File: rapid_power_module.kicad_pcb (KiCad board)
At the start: 4 copper layers, 80 x 136 mm, 209 parts, among them J1 Conn_02x04_Top_Bottom, J10 JST-GH 4Pin, J11 SWD Header, J12 SWD Header, J16 USB_C_Receptacle_USB2.0, J17 TC2050, J2 Conn_02x03_Odd_Even, J3 Conn_02x04_Top_Bottom, J4 Conn_02x03_Odd_Even, J6 Molex MicroFit 2x2, J7 Molex MicroFit 2x2, J8 Molex MicroFit 2x2, J9 Conn_02x04_Top_Bottom, Q1 AOSP21321, Q12 AOSP21321, Q4 HiDRV1, Q5 LoDRV1, Q6 HiDRV2, Q7 LoDRV2, SW1 KMR721NGLFS, SW2 KMR721NGLFS, U1 BQ25756RRVR, U10 L7805, U11 MCP2562-E-SN, U12 STM32F105RCTx, U13 AZ1117I-3.3, U14 TPD4E1U06, U15 TPD4E1U06, U2 CYPD3177-24LQ, U3 BQ76952PFBR, Y3 8MHz 12pF

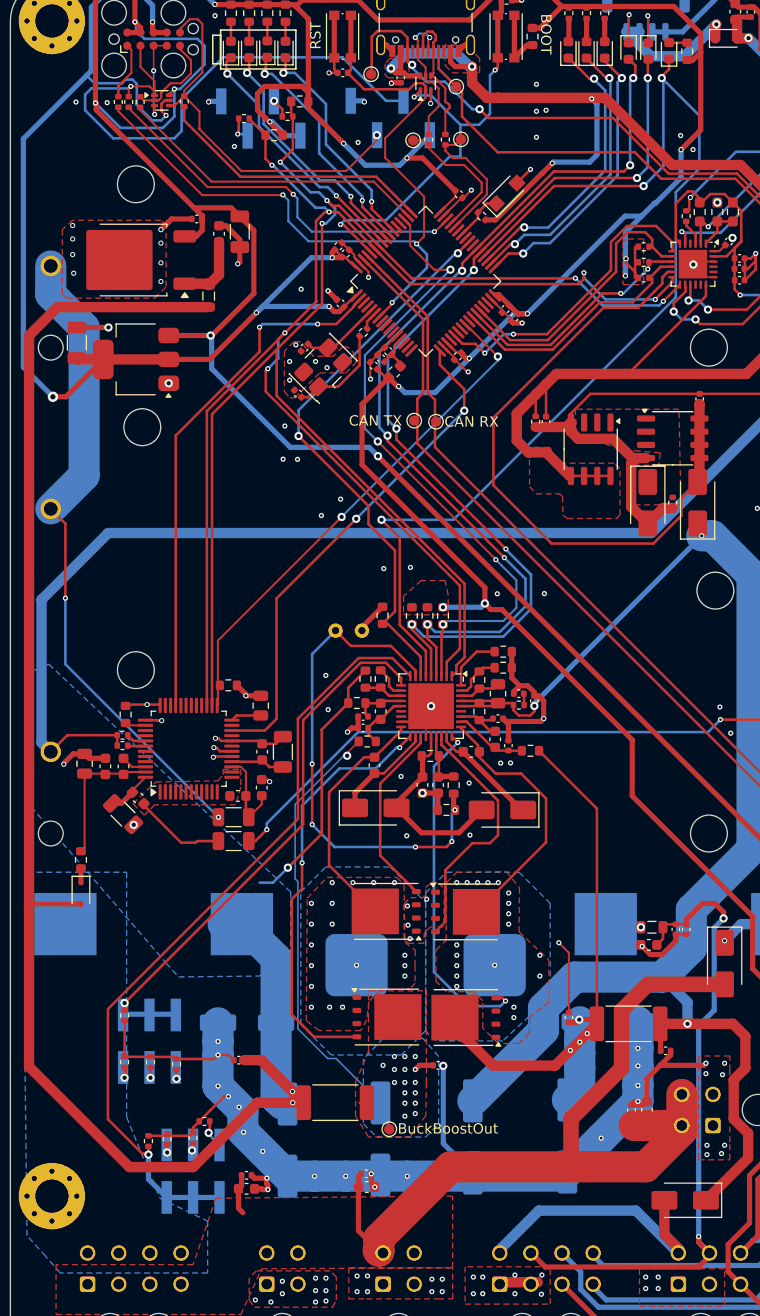
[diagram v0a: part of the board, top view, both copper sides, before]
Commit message: finish routing and silkscreen improvements
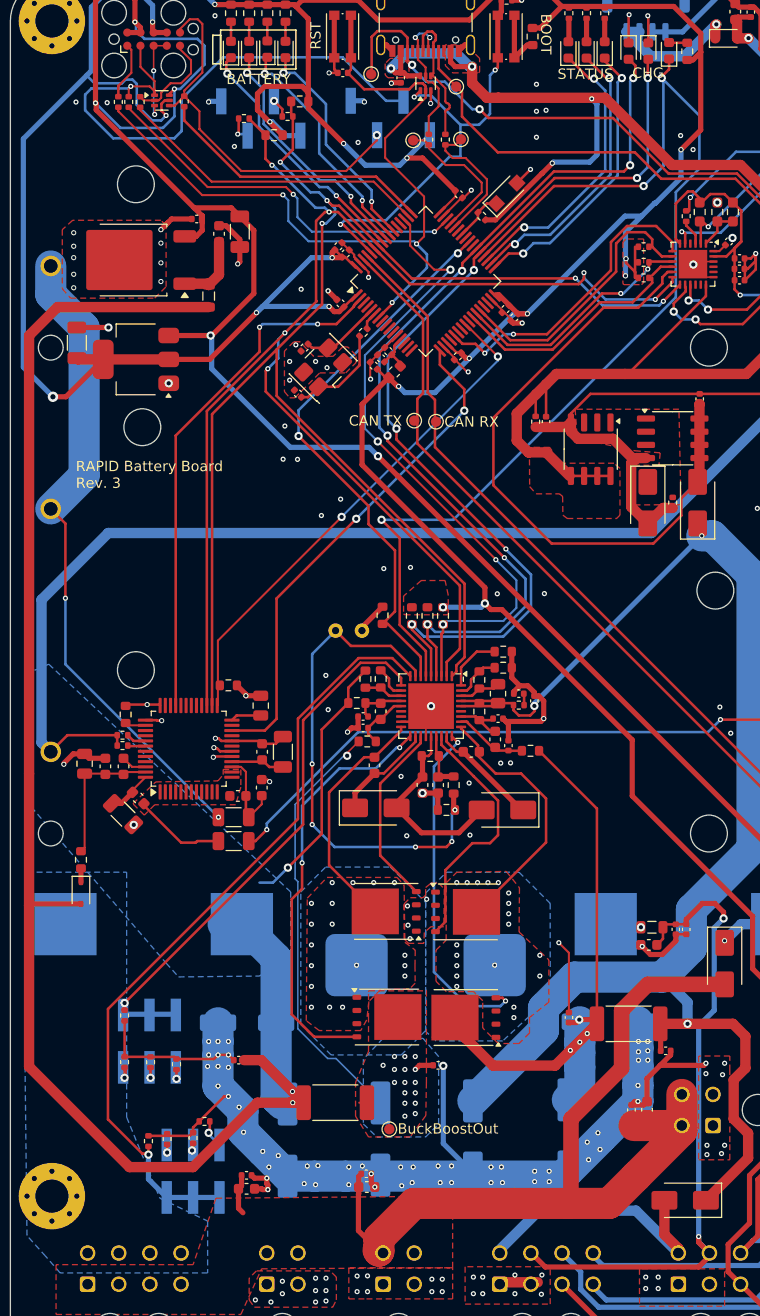
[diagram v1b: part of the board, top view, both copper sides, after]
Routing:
- net +VSW: track 83.2 -> 86.9 mm
- net GND: track 313.2 -> 312.9 mm, vias 155 -> 192
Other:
- board text added: "BATTERY"
- board text added: "CHG"
- board text added: "JLCJLCJLCJLC"
- board text added: "RAPID Battery Board Rev. 3"
- board text added: "STATUS"

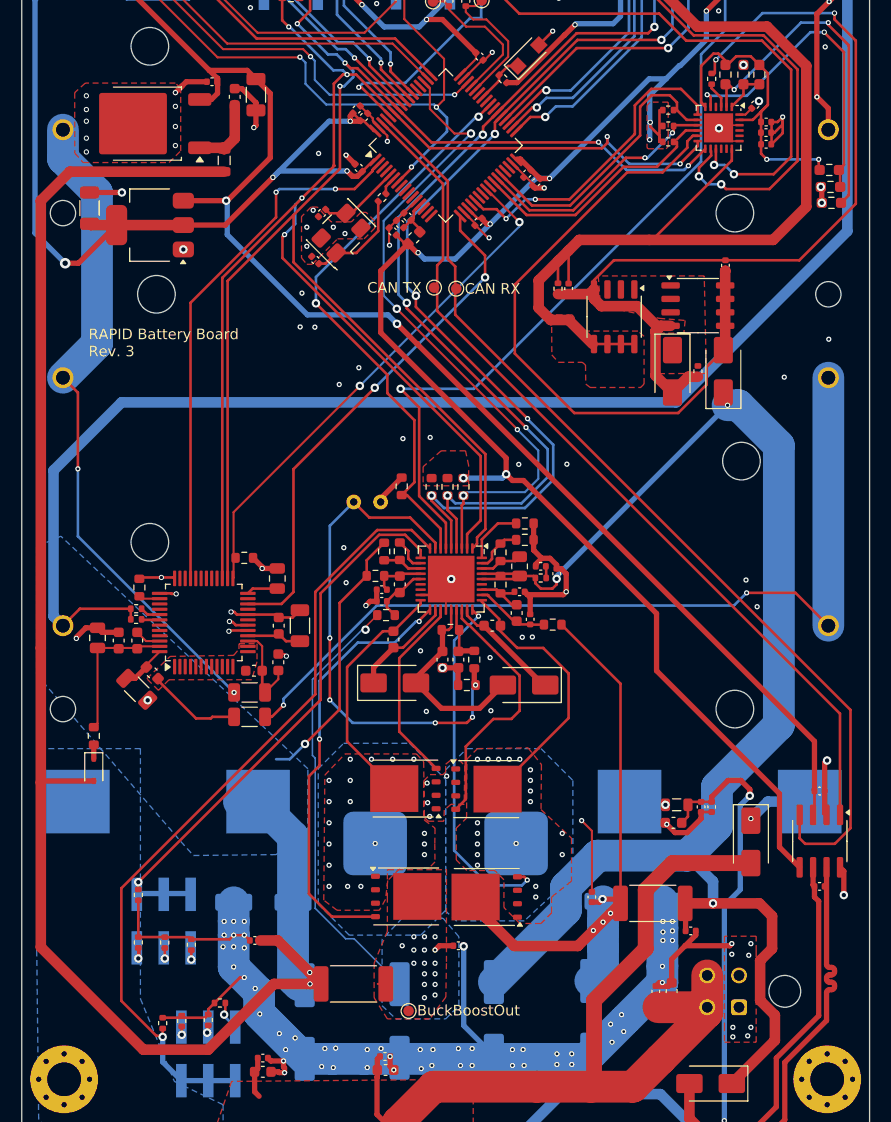
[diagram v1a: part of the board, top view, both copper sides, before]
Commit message: Finishing touches (Zone optimizations to reduce antenna effect, wider battery connection zones)
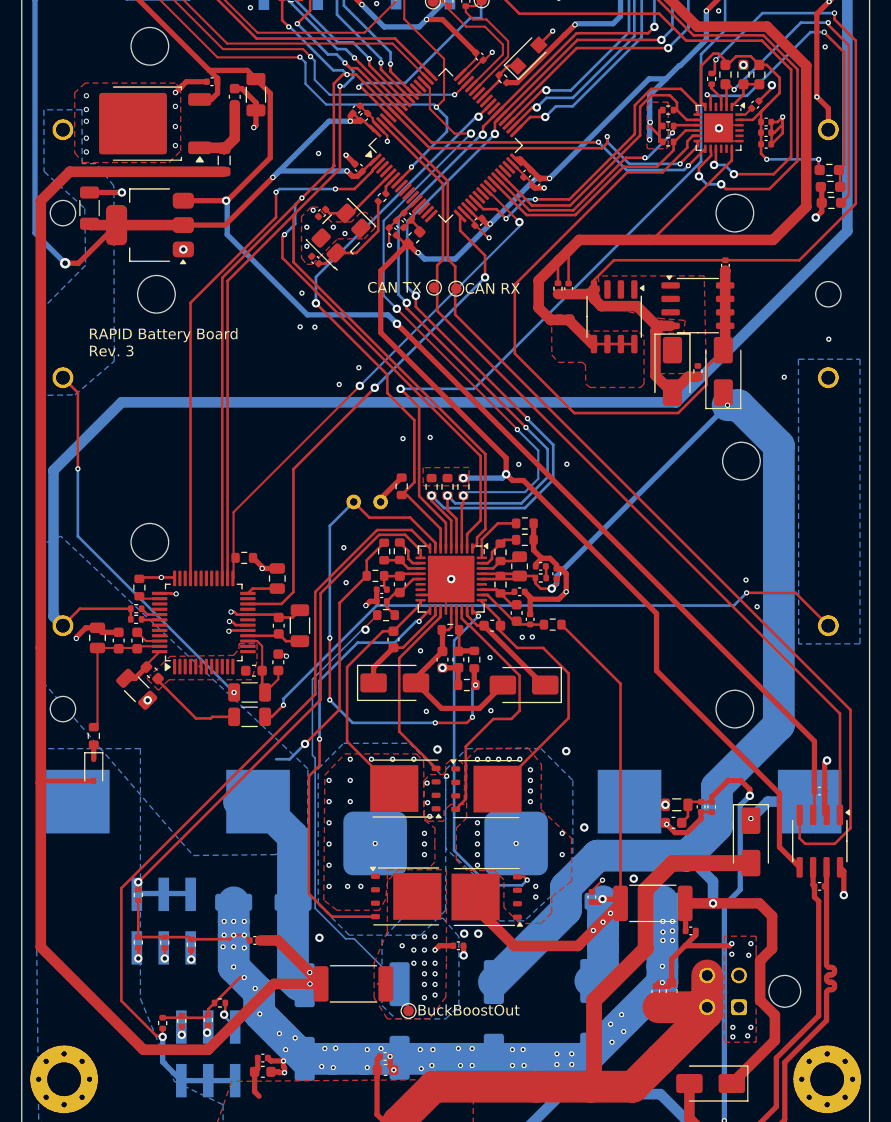
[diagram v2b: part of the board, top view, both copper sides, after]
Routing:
- net Net-(BT2--): track 62.4 -> 36.4 mm
- net Net-(BT1--): track 83.0 -> 59.6 mm
- net GND: track 312.9 -> 300.7 mm, vias 192 -> 198
- net PD_VDDD: track 30.1 -> 31.4 mm
- net V_in: track 143.1 -> 144.2 mm
- added copper zone on B.Cu, net Net-(BT1--)
- added copper zone on B.Cu, net Net-(BT2--)

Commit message: Replace wrong battery manager footprint
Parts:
- R66, R67: footprint Resistor_SMD:R_0603_1608Metric -> Resistor_SMD:R_0402_1005Metric
- U1: footprint Package_DFN_QFN:Texas_RHH0036C_VQFN-36-1EP_6x6mm_P0.5mm_EP4.4x4.4mm -> Package_DFN_QFN:QFN-36-1EP_5x6mm_P0.5mm_EP3.6x4.6mm
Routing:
- net V_in: track 144.2 -> 141.6 mm
- net GND: track 300.7 -> 303.1 mm
- net REGN: track 5.06 -> 5.97 mm
- net ACN: track 7.08 -> 6.27 mm
- net HIDRV1: track 33.4 -> 34.1 mm
- net Net-(J4-Pin_2): track 76.2 -> 76.9 mm
- net LODRV1: track 24.6 -> 25.2 mm
- net PG: track 109.2 -> 109.7 mm
- net Net-(U1-TS): track 48.5 -> 49.1 mm
- net BTST1: track 10.5 -> 11.0 mm
- net CE: track 55.0 -> 55.5 mm
- net STAT2: track 92.5 -> 93.1 mm
- net STAT1: track 89.3 -> 89.8 mm

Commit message: Add basic running embassy loop
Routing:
- added copper zone on F.Cu, net Net-(J9-Pin_5)
- removed copper zone on B.Cu, net Net-(J9-Pin_5)
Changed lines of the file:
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@@
 			(psa4output no)
 			(plot_black_and_white yes)
-			(plotinvisibletext no)
 			(sketchpadsonfab no)
 			(plotpadnumbers no)
@@
 			(keep_text_aligned yes)
 		)
-		(gr_text "40,0000 mm"
+		(gr_text "40.0000 mm"
 			(at 115 13.7 0)
 			(layer "F.Cu")
@@
 			(keep_text_aligned yes)
 		)
-		(gr_text "68,0000 mm"
+		(gr_text "68.0000 mm"
 			(at 87.2 56 90)
 			(layer "F.Cu")
@@
 			(keep_text_aligned yes)
 		)
-		(gr_text "80,0000 mm"
+		(gr_text "80.0000 mm"
 			(at 132.7 166.8 0)
 			(layer "F.Cu")
@@
 			(keep_text_aligned yes)
 		)
-		(gr_text "136,0000 mm"
+		(gr_text "136.0000 mm"
 			(at 63.8 84.199988 90)
 			(layer "F.Cu")
@@
 	)
 	(zone
+		(net 161)
+		(net_name "Net-(J9-Pin_5)")
+		(layer "F.Cu")
+		(hatch edge 0.5)
+		(priority 22)
+		(connect_pads
+			(clearance 0.3)
+		)
+		(min_thickness 0.25)
+		(filled_areas_thickness no)
+		(fill
+			(thermal_gap 0.5)
+			(thermal_bridge_width 0.5)
+		)
+		(polygon
+			(pts
+				(xy 114 146.6) (xy 128.2 146.6) (xy 129.6 145) (xy 131.4 143) (xy 131.581274 127.215076) (xy 131.4 108)
+				(xy 121.8 108) (xy 121.8 131.6) (xy 118.6 139.4) (xy 114 141.6)
+			)
+		)
+	)
+	(zone
 		(net 71)
 		(net_name "GND")
@@
 			)
 		)
-	)
-	(zone
-		(net 161)
-		(net_name "Net-(J9-Pin_5)")
-		(layer "B.Cu")
-		(hatch edge 0.5)
-		(priority 22)
-		(connect_pads
-			(clearance 0.3)
-		)
-		(min_thickness 0.25)
-		(filled_areas_thickness no)
-		(fill yes
-			(thermal_gap 0.5)
-			(thermal_bridge_width 0.5)
-		)
-		(polygon
-			(pts
-				(xy 114 146.6) (xy 99.8 146.6) (xy 98.4 145) (xy 96.6 143) (xy 96.418726 127.215076) (xy 96.6 108)
-				(xy 106.2 108) (xy 106.2 131.6) (xy 109.4 139.4) (xy 114 141.6)
-			)
-		)

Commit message: fix broken trace
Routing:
- added copper zone on B.Cu, net Net-(J9-Pin_5)
- removed copper zone on F.Cu, net Net-(J9-Pin_5)
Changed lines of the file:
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@@
 			(keep_text_aligned yes)
 		)
-		(gr_text "40.0000 mm"
+		(gr_text "40,0000 mm"
 			(at 115 13.7 0)
 			(layer "F.Cu")
@@
 			(keep_text_aligned yes)
 		)
-		(gr_text "68.0000 mm"
+		(gr_text "68,0000 mm"
 			(at 87.2 56 90)
 			(layer "F.Cu")
@@
 			(keep_text_aligned yes)
 		)
-		(gr_text "80.0000 mm"
+		(gr_text "80,0000 mm"
 			(at 132.7 166.8 0)
 			(layer "F.Cu")
@@
 			(keep_text_aligned yes)
 		)
-		(gr_text "136.0000 mm"
+		(gr_text "136,0000 mm"
 			(at 63.8 84.199988 90)
 			(layer "F.Cu")
@@
 	)
 	(zone
-		(net 161)
-		(net_name "Net-(J9-Pin_5)")
-		(layer "F.Cu")
-		(hatch edge 0.5)
-		(priority 22)
-		(connect_pads
-			(clearance 0.3)
-		)
-		(min_thickness 0.25)
-		(filled_areas_thickness no)
-		(fill
-			(thermal_gap 0.5)
-			(thermal_bridge_width 0.5)
-		)
-		(polygon
-			(pts
-				(xy 114 146.6) (xy 128.2 146.6) (xy 129.6 145) (xy 131.4 143) (xy 131.581274 127.215076) (xy 131.4 108)
-				(xy 121.8 108) (xy 121.8 131.6) (xy 118.6 139.4) (xy 114 141.6)
-			)
-		)
-	)
-	(zone
 		(net 71)
 		(net_name "GND")
@@
 			)
 		)
+	)
+	(zone
+		(net 161)
+		(net_name "Net-(J9-Pin_5)")
+		(layer "B.Cu")
+		(hatch edge 0.5)
+		(priority 22)
+		(connect_pads
+			(clearance 0.3)
+		)
+		(min_thickness 0.25)
+		(filled_areas_thickness no)
+		(fill yes
+			(thermal_gap 0.5)
+			(thermal_bridge_width 0.5)
+		)
+		(polygon
+			(pts
+				(xy 112.815384 146.537793) (xy 98.615384 146.537793) (xy 97.215384 144.937793) (xy 95.415384 142.937793)
+				(xy 95.23411 127.152869) (xy 95.415384 107.937793) (xy 105.015384 107.937793) (xy 105.015384 131.537793)
+				(xy 108.215384 139.337793) (xy 112.815384 141.537793)
+			)
+		)

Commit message: added missing footprints and validated all lcsc numbers; started pcb-layouting
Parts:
- removed BT3: Battery_Cell, Inductor Wuerth:BAT_1043
- removed C13, C37, C38, C44, C45: 100n, Capacitor_SMD:C_0402_1005Metric
- removed C20, C65: 1u, Capacitor_SMD:C_0402_1005Metric
- removed C39, C43, C47, C48: 470n, Capacitor_SMD:C_0603_1608Metric
- removed C49: 47n, Capacitor_SMD:C_0603_1608Metric
- removed C86, C90: 10u, Capacitor_SMD:C_0603_1608Metric
- removed C87, C91: 10n, Capacitor_SMD:C_0402_1005Metric
- removed D16, D21, D23, D7: green, LED_SMD:LED_0603_1608Metric
- removed D20: yellow, LED_SMD:LED_0603_1608Metric
- removed D22: red, LED_SMD:LED_0603_1608Metric
- removed D24: Vz = 3.6V, Diode_SMD:Nexperia_CFP3_SOD-123W
- removed D9: ~, Diode_SMD:D_SOD-323
- removed FB3: 120R, Inductor_SMD:L_0805_2012Metric
- removed J10: JST-GH 4Pin, Connector_JST:JST_GH_SM04B-GHS-TB_1x04-1MP_P1.25mm_Horizontal
- removed J11: SWD Header, Connector_PinHeader_2.54mm:PinHeader_1x04_P2.54mm_Vertical_SMD_Pin1Left
- removed J16: USB_C_Receptacle_USB2.0, Connector_USB:USB_C_Receptacle_Palconn_UTC16-G
- removed J8: Molex MicroFit 2x2, Connector_Molex:Molex_Micro-Fit_3.0_43045-0400_2x02_P3.00mm_Horizontal
- removed J9: Conn_02x04_Top_Bottom, Connector_Molex:Molex_Micro-Fit_3.0_43045-0800_2x04_P3.00mm_Horizontal
- removed Q12: AOSP21321, Package_SO:SO-8_3.9x4.9mm_P1.27mm
- removed Q4: HiDRV1, Package_TO_SOT_SMD:TDSON-8-1
- removed Q5: LoDRV1, Package_TO_SOT_SMD:TDSON-8-1
- removed Q6: HiDRV2, Package_TO_SOT_SMD:TDSON-8-1
- removed Q7: LoDRV2, Package_TO_SOT_SMD:TDSON-8-1
- removed R19, R48: 0R, Resistor_SMD:R_0603_1608Metric_Pad0.98x0.95mm_HandSolder
- removed R20: 20, Resistor_SMD:R_1206_3216Metric
- removed R21: 100, Resistor_SMD:R_0603_1608Metric
- removed R22: 10R, Resistor_SMD:R_0603_1608Metric
- removed R23: 4k7, Resistor_SMD:R_0603_1608Metric
- removed R24: 100k, Resistor_SMD:R_0603_1608Metric
- removed R25, R94, R97: 20k, Resistor_SMD:R_0402_1005Metric
- removed R27: 50k, Resistor_SMD:R_0402_1005Metric
- removed R28: 250k, Resistor_SMD:R_0603_1608Metric
- removed R31: 50k, Resistor_SMD:R_0603_1608Metric
- removed R33: 300k, Resistor_SMD:R_0603_1608Metric
- removed R37, R41, R79, R80: 10, Resistor_SMD:R_0603_1608Metric
- removed R38, R65: 5m, Resistor_SMD:R_2512_6332Metric_Pad1.40x3.35mm_HandSolder
- removed R39, R45: 4k7, Resistor_SMD:R_0402_1005Metric
- removed R40, R42, R46, R95: 10k, Resistor_SMD:R_0402_1005Metric
- removed R43: 68k, Resistor_SMD:R_0603_1608Metric
- removed R44: 1000k, Resistor_SMD:R_0805_2012Metric
- removed R47: dnp, Resistor_SMD:R_0603_1608Metric_Pad0.98x0.95mm_HandSolder
- removed R64, R69, R70, R72, R91: 10k, Resistor_SMD:R_0603_1608Metric
- removed R73, R75: 22R, Resistor_SMD:R_0402_1005Metric
- removed R83: 49k9, Resistor_SMD:R_0402_1005Metric
- removed R89, R90: 1k, Resistor_SMD:R_0402_1005Metric
- removed R96: 5k1, Resistor_SMD:R_0402_1005Metric
- removed R98: 15k, Resistor_SMD:R_0402_1005Metric
- removed TP1: BuckBoostOut, TestPoint:TestPoint_Pad_D1.0mm
- removed TP2: TP_CAN_TX, TestPoint:TestPoint_Pad_D1.0mm
- removed TP3: TP_CAN_RX, TestPoint:TestPoint_Pad_D1.0mm
- removed TP4: TP_USB_D+, TestPoint:TestPoint_Pad_D1.0mm
- removed TP5: TP_USB_D-, TestPoint:TestPoint_Pad_D1.0mm
- removed TP6: TP_USB_CC2, TestPoint:TestPoint_Pad_D1.0mm
- removed TP7: TP_USB_CC1, TestPoint:TestPoint_Pad_D1.0mm
- removed U14: TPD4E1U06, Package_TO_SOT_SMD:SOT-563
- removed U3: BQ76952PFBR, Package_QFP:TQFP-48_7x7mm_P0.5mm
- added BT4: Battery_Cell, Inductor Wuerth:BAT_1043, B.Cu at (123.7, 108.8)
- added C27: 10u, Capacitor_SMD:C_0603_1608Metric, F.Cu at (391.6, 12.6)
- added C28: 10u, Capacitor_SMD:C_0603_1608Metric, F.Cu at (-1.82, 233.2)
- added C29: 10n, Capacitor_SMD:C_0402_1005Metric, F.Cu at (-2.09, 229.8)
- added C30: 100n, Capacitor_SMD:C_0402_1005Metric, F.Cu at (387.6, 18.1)
- added C31: 10u, Capacitor_SMD:C_0603_1608Metric, F.Cu at (391.6, 11.0)
- added C32: 10u, Capacitor_SMD:C_0603_1608Metric, F.Cu at (391.6, 9.45)
- added C33: 10u, Capacitor_SMD:C_0603_1608Metric, F.Cu at (391.6, 7.90)
- added C34: 10u, Capacitor_SMD:C_0603_1608Metric, F.Cu at (391.6, 6.35)
- added D10: ~, Diode_SMD:D_SMA, F.Cu at (122.3, -77.2)
- added D3: green, LED_SMD:LED_0805_2012Metric, F.Cu at (160.5, -70.0)
- added F2: 20A, Fuse:Fuseholder_Cylinder-5x20mm_Wuerth_696103101002-SMD_Horizontal_Open, F.Cu at (135.7, 114.8)
- added J5: Molex MicroFit 2x2, Connector_Molex:Molex_Micro-Fit_3.0_43045-0400_2x02_P3.00mm_Horizontal, B.Cu at (156.0, 125.0)
- added Q2: NMOS, Package_TO_SOT_THT:TO-220-3_Horizontal_TabDown, F.Cu at (387.9, 23.4)
- added R10: 1k, Resistor_SMD:R_0402_1005Metric, F.Cu at (155.7, -65.8)
- added R13: 1k, Resistor_SMD:R_0402_1005Metric, F.Cu at (162.8, -68.0)
- added R_IN1: 75, Resistor_SMD:R_0603_1608Metric, F.Cu at (-52.1, 71.9)
- added R_IN2: 75, Resistor_SMD:R_0603_1608Metric, F.Cu at (-51.4, 74.1)
- added R_IN3: 75, Resistor_SMD:R_0603_1608Metric, F.Cu at (-51.4, 77.2)
- added R_IN4: 75, Resistor_SMD:R_0603_1608Metric, F.Cu at (-51.4, 80.2)
- added R_LD1: 453k, Resistor_SMD:R_0402_1005Metric, F.Cu at (-42.2, 76.0)
- added R_SNS1: 1m, Resistor_SMD:R_2512_6332Metric, F.Cu at (-46.7, 79.8)
- added R_TS_PU1: 10k, Resistor_SMD:R_0402_1005Metric, F.Cu at (-42.2, 73.3)
- C10, C11: value 1u -> 100n
- C14: value 220n -> 2.2u; footprint Capacitor_SMD:C_0603_1608Metric -> Capacitor_SMD:C_0805_2012Metric
- C15: value 220n -> 100n; footprint Capacitor_SMD:C_0603_1608Metric -> Capacitor_SMD:C_0402_1005Metric
- C16: value 220n -> 1n; footprint Capacitor_SMD:C_0603_1608Metric -> Capacitor_SMD:C_0402_1005Metric
- C17: value 220n -> 1u; footprint Capacitor_SMD:C_0603_1608Metric -> Capacitor_SMD:C_0402_1005Metric
- C18: value 470n -> 1u; footprint Capacitor_SMD:C_0603_1608Metric -> Capacitor_SMD:C_0402_1005Metric
- C19: value 1u -> 100n; footprint Capacitor_SMD:C_0805_2012Metric -> Capacitor_SMD:C_0402_1005Metric
- C2, C4, C5: value 82u -> 10u; footprint Capacitor_SMD:CP_Elec_8x6.9 -> Capacitor_SMD:C_0603_1608Metric; moved to F.Cu
- C21: value 2u2 -> 100n; footprint Capacitor_SMD:C_0805_2012Metric -> Capacitor_SMD:C_0402_1005Metric
- C22: value 0.47uF -> 100n
- C23: value 3u3 -> 10u; footprint Capacitor_SMD:C_0402_1005Metric -> Capacitor_SMD:C_0603_1608Metric
- C24: value 100p -> 100n; footprint Capacitor_SMD:C_0603_1608Metric -> Capacitor_SMD:C_0402_1005Metric
- C26: value 100n -> 4u7
- C3: value 100n -> 10u; footprint Capacitor_SMD:C_0402_1005Metric -> Capacitor_SMD:C_0603_1608Metric
- C58: value 470n -> 330n
- C6: value 82u -> 100n; footprint Capacitor_SMD:CP_Elec_8x6.9 -> Capacitor_SMD:C_0402_1005Metric; moved to F.Cu
- C7, C8: footprint Capacitor_SMD:CP_Elec_6.3x5.9 -> Capacitor_SMD:C_0603_1608Metric; moved to F.Cu
- C9: value 1u -> 47n; footprint Capacitor_SMD:C_0402_1005Metric -> Capacitor_SMD:C_0603_1608Metric
- D1: value D -> 12V; footprint Diode_SMD:D_SMA -> Diode_SMD:D_SOD-523
- D18, D19, D5: footprint LED_SMD:LED_0603_1608Metric -> LED_SMD:LED_0805_2012Metric
- D2: value D -> red; footprint Diode_SMD:D_SMA -> LED_SMD:LED_0603_1608Metric
- D4: value ~ -> green; footprint Diode_SMD:D_SOD-323 -> LED_SMD:LED_0805_2012Metric
- D6: value ~ -> green; footprint Diode_SMD:D_SMA -> LED_SMD:LED_0805_2012Metric
- F1: moved to F.Cu
- F3: value 20A -> 5A; moved to F.Cu
- J17: moved to B.Cu
- J2, J4: value Conn_02x03_Odd_Even -> Molex MicroFit 2x2; footprint Connector_PinHeader_2.54mm:PinHeader_2x03_P2.54mm_Vertical_SMD -> Connector_Molex:Molex_Micro-Fit_3.0_43045-0400_2x02_P3.00mm_Horizontal; moved to F.Cu
- L2: value 5u6 -> 1u; footprint Inductor Wuerth:Wuerth 7443557560 -> Inductor_SMD_Wurth:L_Wurth_WE-LQSH-3012; moved to F.Cu
- Q1: value AOSP21321 -> NMOS; footprint Package_SO:SO-8_3.9x4.9mm_P1.27mm -> Package_TO_SOT_THT:TO-220-3_Horizontal_TabDown
- R1: value 2.4 -> 2; footprint Resistor_SMD:R_0402_1005Metric -> Resistor_SMD:R_0603_1608Metric
- R11, R12: value 20 -> 1k; footprint Resistor_SMD:R_1206_3216Metric -> Resistor_SMD:R_0402_1005Metric
- R14, R15, R16, R34: footprint Resistor_SMD:R_0603_1608Metric -> Resistor_SMD:R_0402_1005Metric
- R17: value 1k -> 100
- R18: value dnp -> 100; footprint Resistor_SMD:R_0603_1608Metric_Pad0.98x0.95mm_HandSolder -> Resistor_SMD:R_0603_1608Metric
- R2: value 20 -> 10k5; footprint Resistor_SMD:R_1206_3216Metric -> Resistor_SMD:R_0603_1608Metric
- R3: value 35k -> 10k5
- R32: value 4k -> 5k24
- R4: value 10k -> 294; footprint Resistor_SMD:R_0402_1005Metric -> Resistor_SMD:R_0603_1608Metric
- R5: value 1k -> 100; footprint Resistor_SMD:R_0402_1005Metric -> Resistor_SMD:R_0603_1608Metric
- R6: value 0R -> 20k; footprint Resistor_SMD:R_0603_1608Metric_Pad0.98x0.95mm_HandSolder -> Resistor_SMD:R_0603_1608Metric
- R66, R67: value 4.7k -> 10k
- R7: value dnp -> 2k2; footprint Resistor_SMD:R_0603_1608Metric_Pad0.98x0.95mm_HandSolder -> Resistor_SMD:R_0603_1608Metric
- R8: value 49k9 -> 1k
- R82: value 22k -> 30k31; footprint Resistor_SMD:R_0603_1608Metric -> Resistor_SMD:R_0805_2012Metric
- SW1, SW2: value KMR721NGLFS -> TS342A2P; footprint Button_Switch_SMD:SW_Push_1P1T_NO_CK_KMR2 -> Button_Switch_SMD:SW_Push_SPST_NO_Alps_SKRK
- TH1: footprint Resistor_THT:R_Axial_DIN0204_L3.6mm_D1.6mm_P2.54mm_Vertical -> Resistor_SMD:R_0603_1608Metric; moved to F.Cu
- U1: value BQ25756RRVR -> BQ7791500PWR; footprint Package_DFN_QFN:QFN-36-1EP_5x6mm_P0.5mm_EP3.6x4.6mm -> Package_SO:TSSOP-24_4.4x7.8mm_P0.65mm
- U2: value CYPD3177-24LQ -> BQ25798RQMR; footprint Package_DFN_QFN:QFN-24-1EP_4x4mm_P0.5mm_EP2.75x2.75mm -> BQ25798:IC_BQ25798RQMR
- moved C3 300.0 mm to (396.1, 16.1), turned to 0 degrees
- moved C5 298.0 mm to (396.1, 17.6), turned to 0 degrees
- moved R2 296.1 mm to (390.7, 21.5), turned to 0 degrees
- moved C8 291.9 mm to (388.6, 13.6)
- moved C14 288.7 mm to (384.8, 21.1), turned to 180 degrees
- moved C16 287.7 mm to (394.1, 14.8), turned to 180 degrees
- moved C6 287.2 mm to (391.6, 13.8), turned to 180 degrees
- moved C2 277.8 mm to (388.6, 10.5), turned to 180 degrees
- moved R3 277.5 mm to (398.5, 16.9)
- moved TH1 277.2 mm to (396.2, 21.2)
- moved C26 274.6 mm to (387.6, 16.2), turned to 90 degrees
- moved L2 272.2 mm to (385.1, 9.50), turned to 0 degrees
- moved R82 272.2 mm to (396.4, 19.4), turned to 0 degrees
- moved C46 271.1 mm to (385.5, 6.90), turned to 0 degrees
- moved D2 270.1 mm to (385.5, 13.7), turned to 180 degrees
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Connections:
- net /J1-SWCLK renamed /Controller and Logic/J1-SWCLK
- net /J1-SWDIO renamed /Controller and Logic/J1-SWDIO
- net /J1-SWO renamed /Controller and Logic/J1-SWO
- net CAN_2_H renamed Net-(J1-Pin_8)
- net CAN_2_L renamed Net-(J1-Pin_4)
- BT1 pad P: PACK+ -> Net-(BT1-+)
- BT2 pad N: Net-(BT2--) -> BAL_GND
- C1 pad 1: Net-(C1-Pad1) -> /Charger/V_in
- C10 pad 1: USB_PD_OUT -> Net-(U1A-SRN)
- C10 pad 2: Net-(D12-A) -> BAL_GND
- C11 pad 1: PD_VDDD -> BAL_GND
- C11 pad 2: GND -> Net-(U1A-SRP)
- C12 pad 1: PD_VDDD -> Net-(U1A-SRP)
- C12 pad 2: GND -> Net-(U1A-SRN)
- C14 pad 1: CELL 3 -> Net-(C14-Pad1)
- C14 pad 2: CELL 2 -> GND
- C15 pad 1: CELL 2 -> +5V
- C15 pad 2: CELL 1 -> GND
- C16 pad 1: CELL 1 -> GND
- C16 pad 2: GND -> Net-(U2-SDRV)
- C17 pad 1: GND -> Net-(U1B-VDD)
- C17 pad 2: CELL 0 -> BAL_GND
- C18 pad 1: Net-(U3-CP1) -> Net-(U1B-AVDD)
- C18 pad 2: /VCC_BQ76952 -> BAL_GND
- C19 pad 1: GND -> BAT3
- C19 pad 2: /VCC_BQ76952 -> BAT2
- C2 pad 1: V_in -> Net-(U2-PMID)
- C21 pad 1: GND -> BAT2
- C21 pad 2: Net-(U3-REG18) -> BAT1
- C22 pad 1: V_in -> BAT1
- C22 pad 2: GND -> BAL_GND
- C23 pad 1: GND -> Net-(U2-PMID)
- C23 pad 2: /VBUS -> GND
- C24 pad 1: GND -> BAL_GND
- C24 pad 2: /VCC_BQ76952 -> BAT0
- C25 pad 1: /V_in_post_sense -> Net-(U2-PMID)
- C26 pad 1: BuckBoostOut -> REGN
- C3 pad 1: PACK+ -> V_BAT
- C4 pad 1: /V_in_post_sense -> Net-(Q2-D)
- C46 pad 1: SW2 -> Net-(U2-BTST1)
- C46 pad 2: BTST2 -> Net-(U2-SW1)
- C5 pad 1: PACK+ -> V_BAT
- C58 pad 2: Net-(U10-IN) -> Net-(D10-K)
- C6 pad 1: BuckBoostOut -> /Charger/SYS+
- C7 pad 1: /V_in_post_sense -> Net-(Q2-D)
- C8 pad 1: PACK+ -> Net-(U2-PMID)
- C9 pad 1: /VBUS -> Net-(U2-BTST2)
- C9 pad 2: Net-(D12-A) -> Net-(U2-SW2)
- D1 pad 1: BTST1 -> Net-(D1-K)
- D1 pad 2: DRV_SUP -> Net-(D1-A)
- D11 pad 2: +VSW -> Net-(D11-A)
- D12 pad 1: /MFS -> /Charger/V_in
- D2 pad 1: BTST2 -> Net-(D2-K)
- D2 pad 2: DRV_SUP -> Net-(D2-A)
- D4 pad 1: Net-(D4-K) -> CHRG_IND_LED_2
- D4 pad 2: PACK+ -> Net-(D4-A)
- D5 pad 1: CHRG_IND_LED_1 -> CHRG_IND_LED_3
- D6 pad 1: V_in -> CHRG_IND_LED_4
- D6 pad 2: charging_voltage -> Net-(D6-A)
- D8 pad 1: V_in -> Net-(D10-K)
- D8 pad 2: USB_PD_OUT -> main_voltage
- F3 pad 1: Net-(J9-Pin_5) -> Net-(D12-A)
- F3 pad 2: PACK+ -> charging_voltage
- J2 pad 1: Net-(J2-Pin_1) -> GND
- J2 pad 2: Net-(J2-Pin_2) -> GND
- J2 pad 3: Net-(J2-Pin_3) -> +VSW
- J2 pad 4: Net-(J2-Pin_2) -> +VSW
- J4 pad 1: Net-(J4-Pin_1) -> /Charger/SYS+
- J4 pad 2: Net-(J4-Pin_2) -> /Charger/SYS+
- J4 pad 3: Net-(J4-Pin_3) -> GND
- J4 pad 4: Net-(J4-Pin_2) -> GND
- L2 pad 1: SW1 -> Net-(U2-SW2)
- L2 pad 2: SW2 -> Net-(U2-SW1)
- Q1 pad 1: /MFS -> /Charger/V_in
- Q1 pad 2: /MFS -> Net-(D1-K)
- Q1 pad 3: /MFS -> Net-(D1-A)
- R1 pad 1: Net-(C1-Pad1) -> Net-(C14-Pad1)
- R1 pad 2: V_in -> /Charger/V_in
- R11 pad 1: Net-(BT1--) -> +3V3
- R11 pad 2: CELL 2 -> Net-(D19-A)
- R12 pad 1: Net-(BT2--) -> +3V3
- R12 pad 2: CELL 1 -> Net-(D3-A)
- R15 pad 2: Net-(D7-A) -> Net-(D6-A)
- R16 pad 1: +3V3 -> Net-(U1A-PRES)
- R16 pad 2: Net-(D16-A) -> V_BAT
- R17 pad 1: +3V3 -> BAL_GND
- R17 pad 2: Net-(D23-A) -> Net-(U1A-SRP)
- R18 pad 1: PD_VDDD -> GND
- R18 pad 2: VBUS_MIN -> Net-(U1A-SRN)
- R2 pad 1: PACK+ -> GND
- R2 pad 2: CELL 3 -> Net-(U2-QON_N)
- R3 pad 1: Net-(U1-FBG) -> GND
- R3 pad 2: Net-(U1-FB) -> Net-(U2-PROG)
- R32 pad 1: Net-(U1-TS) -> Net-(U2-TS)
- R4 pad 1: /VBUS -> Net-(D1-K)
- R4 pad 2: Net-(D12-A) -> Net-(U2-ACDRV1)
- R5 pad 1: Net-(D12-A) -> V_BAT
- R5 pad 2: VBUS_FET_EN -> Net-(U2-BATP)
- R6 pad 1: PD_VDDD -> GND
- R6 pad 2: VBUS_MAX -> /Charger/CE_N
- R66 pad 1: I2C_SDA -> I2C1_SDA
- R67 pad 1: I2C_SCL -> I2C1_SCL
- R7 pad 1: VBUS_MAX -> REGN
- R7 pad 2: GND -> Net-(D2-A)
- R77 pad 1: I2C_SDA -> I2C1_SDA
- R78 pad 1: I2C_SCL -> I2C1_SCL
- R8 pad 1: /MFS -> V_BAT
- R8 pad 2: Net-(D12-A) -> Net-(U1B-VDD)
- R82 pad 1: Net-(U1-TS) -> Net-(U2-TS)
- R9 pad 1: Net-(U3-LD) -> /Charger/INT
- R9 pad 2: PACK+ -> +3V3
- TH1 pad 1: Net-(U1-TS) -> Net-(U2-TS)
- U1 pad 1: I2C_SCL -> Net-(U1B-VDD)
- U1 pad 10: Net-(J2-Pin_2) -> Net-(U1A-SRP)
- U1 pad 11: Net-(U1-FBG) -> Net-(U1A-SRN)
- U1 pad 12: Net-(U1-FB) -> unconnected-(U1A-DSG-Pad12)
- U1 pad 13: SRN -> unconnected-(U1A-CHG-Pad13)
- U1 pad 14: SRP -> Net-(U1A-LD)
- U1 pad 16: unconnected-(U1-NC-Pad16) -> BAL_GND
- U1 pad 17: GND -> unconnected-(U1A-OCDP-Pad17)
- U1 pad 18: SW2 -> Net-(U1A-TS)
- U1 pad 19: HIDRV2 -> unconnected-(U1A-VTB-Pad19)
- U1 pad 2: I2C_SDA -> Net-(U1B-AVDD)
- U1 pad 20: BTST2 -> BAL_GND
- U1 pad 21: LODRV2 -> unconnected-(U1A-CBO-Pad21)
- U1 pad 22: GND -> Net-(U1A-PRES)
- U1 pad 23: DRV_SUP -> BAL_GND
- U1 pad 24: REGN -> BAL_GND
- U1 pad 3: INT -> BAT3
- U1 pad 4: STAT1 -> BAT3
- U1 pad 5: STAT2 -> BAT3
- U1 pad 6: PG -> BAT2
- U1 pad 7: CE -> BAT1
- U1 pad 8: Net-(U1-TS) -> BAT0
- U1 pad 9: Net-(J4-Pin_2) -> BAL_GND
- U10 pad 1: Net-(U10-IN) -> Net-(D10-K)
- U12 pad 17: TS2 -> unconnected-(U12-PA3-Pad17)
- U12 pad 2: RST_SHUT -> unconnected-(U12-PC13-Pad2)
- U12 pad 21: USB_PD_INTERRUPT -> unconnected-(U12-PA5-Pad21)
- U12 pad 24: BAL_ALERT -> unconnected-(U12-PC4-Pad24)
- U12 pad 26: FLIP -> unconnected-(U12-PB0-Pad26)
- U12 pad 27: FAULT -> unconnected-(U12-PB1-Pad27)
- U12 pad 28: GPIO_1 -> CHRG_IND_LED_4
- U12 pad 36: PG -> unconnected-(U12-PB15-Pad36)
- U12 pad 37: STAT2 -> unconnected-(U12-PC6-Pad37)
- U12 pad 38: STAT1 -> unconnected-(U12-PC7-Pad38)
- U12 pad 40: CE -> /Charger/CE_N
- U12 pad 42: USB_FS_VBUS -> unconnected-(U12-PA9-Pad42)
- U12 pad 44: USB_D- -> unconnected-(U12-PA11-Pad44)
- U12 pad 45: USB_D+ -> unconnected-(U12-PA12-Pad45)
- U12 pad 51: INT -> /Charger/INT
- U12 pad 57: CHRG_IND_LED_4 -> CAN_RX
- U12 pad 58: I2C_SCL -> CAN_TX
- U12 pad 59: I2C_SDA -> I2C1_SDA
- U12 pad 61: CAN_RX -> I2C1_SCL
- U12 pad 62: CAN_TX -> unconnected-(U12-PB9-Pad62)
- U2 pad 1: VBUS_MIN -> Net-(D2-K)
- U2 pad 10: FLIP -> GND
- U2 pad 11: USB_PD_OUT -> Net-(U2-ACDRV1)
- U2 pad 12: I2C_SDA -> Net-(U2-QON_N)
- U2 pad 13: I2C_SCL -> /Charger/CE_N
- U2 pad 14: CC2 -> I2C1_SCL
- U2 pad 15: CC1 -> I2C1_SDA
- U2 pad 16: unconnected-(U2-NC-Pad16) -> Net-(U2-TS)
- U2 pad 17: unconnected-(U2-NC-Pad17) -> REGN
- U2 pad 18: /VBUS -> Net-(U2-BATP)
- U2 pad 19: GND -> Net-(U2-BTST2)
- U2 pad 2: VBUS_MAX -> Net-(Q2-D)
- U2 pad 20: unconnected-(U2-NC-Pad20) -> Net-(U2-PROG)
- U2 pad 21: unconnected-(U2-NC-Pad21) -> /Charger/INT
- U2 pad 22: GND -> V_BAT
- U2 pad 23: PD_VDDD -> V_BAT
- U2 pad 24: Net-(U2-VCCD) -> Net-(U2-SDRV)
- U2 pad 25: GND -> /Charger/SYS+
- U2 pad 3: VBUS_FET_EN -> Net-(Q2-D)
- U2 pad 4: unconnected-(U2-SAFE_PWR_EN-Pad4) -> Net-(U2-BTST1)
- U2 pad 5: ISNK_COARSE -> REGN
- U2 pad 6: PD_VDDD -> unconnected-(U2-D+-Pad6)
- U2 pad 7: USB_PD_INTERRUPT -> unconnected-(U2-D--Pad7)
- U2 pad 8: GPIO_1 -> Net-(Q2-D)
- U2 pad 9: FAULT -> /Charger/V_in
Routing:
- net +3V3: track 382.2 -> 18.4 mm, vias 18 -> 2
- net PACK+: track 337.3 -> 0.00 mm, vias 5 -> 0
- net GND: track 303.1 -> 18.5 mm, vias 198 -> 10
- net +5V: track 172.2 -> 7.15 mm, vias 5 -> 1
- net I2C_SDA: track 147.2 -> 0.00 mm, vias 6 -> 0
- net I2C_SCL: track 145.5 -> 0.00 mm, vias 5 -> 0
- net /VBUS: track 143.9 -> 0.00 mm, vias 4 -> 0
- net V_in: track 141.6 -> 0.00 mm, vias 3 -> 0
- net PG: track 109.7 -> 0.00 mm, vias 3 -> 0
- net STAT2: track 93.1 -> 0.00 mm, vias 6 -> 0
- net CAN_RX: track 92.8 -> 0.00 mm
- net STAT1: track 89.8 -> 0.00 mm, vias 6 -> 0
- net +VSW: track 86.9 -> 0.00 mm
- net Net-(D12-A): track 84.5 -> 0.00 mm, vias 2 -> 0
- net CAN_TX: track 83.6 -> 0.00 mm
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- added copper zone on B.Cu, net GND
- removed copper zone on F.Cu, net +3V3
- removed copper zone on F.Cu, net +VSW
- removed copper zone on F.Cu, net /MFS
- removed copper zone on F.Cu, net /VBUS
- removed copper zone on B.Cu, net BuckBoostOut
- removed copper zone on F.Cu, net BuckBoostOut
- removed copper zone on F.Cu, net CELL 2
- removed copper zone on F.Cu, net GND
- removed copper zone on In1.Cu, net GND
- removed copper zone on In2.Cu, net GND
- removed copper zone on B.Cu, net Net-(BT1--)
- removed copper zone on B.Cu, net Net-(BT2--)
- removed copper zone on B.Cu, net Net-(J9-Pin_5)
- removed copper zone on B.Cu, net PACK+
- removed copper zone on B.Cu, net SW1
- removed copper zone on F.Cu, net SW1
- removed copper zone on B.Cu, net SW2
- removed copper zone on F.Cu, net SW2
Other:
- board size 80 x 136 mm -> 97 x 82 mm
- board text added: "Arming"
- board text added: "Balancer"
- board text added: "Charger"
- board text added: "Common"
- board text added: "HCO"
- board text added: "MCU"
- board text added: "Vehicle Bus"
- board text removed: "+"
- board text removed: "-"
- board text removed: "BAT 1"
- board text removed: "BAT 2"
- board text removed: "BAT 3"
- board text removed: "BATTERY"
- board text removed: "BOOT"
- board text removed: "BuckBoostOut"
- board text removed: "CAN RX"
- board text removed: "CAN TX"
- board text removed: "CHG"
- board text removed: "EN"
- board text removed: "JLCJLCJLCJLC"
- board text removed: "PW"
- board text removed: "PW (Max 3A)"
- board text removed: "PW SPCB"
- board text removed: "RAPID Battery Board Rev. 3"
- board text removed: "RST"
- board text removed: "STATUS"
- board text removed: "SYS fuse"
- board text removed: "VB"
- board text removed: "VB fuse"

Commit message: started routing Please enter the commit message for your changes. Lines starting
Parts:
- removed D1: 12V, Diode_SMD:D_SOD-523
- removed Q1, Q2: NMOS, Package_TO_SOT_THT:TO-220-3_Horizontal_TabDown
- removed R4: 294, Resistor_SMD:R_0603_1608Metric
- BT1, BT2, BT4, J1, J12, J17, J3, J5, J6, J7: moved to F.Cu
- C1, C10, C11, C12, C14, C15, C16, C17, C18, C19, C2, C21, C22, C23, C24, C25, C26, C27, C28, C29, C3, C30, C31, C32, C33, C34, C4, C46, C5, C58, C6, C60, C61, C63, C67, C68, C69, C7, C70, C71, C72, C73, C74, C75, C76, C77, C78, C79, C8, C80, C81, C82, C83, C84, C85, C88, C89, C9, D10, D11, D12, D17, D18, D19, D2, D3, D4, D5, D6, D8, F1, F2, F3, FB1, FB2, L2, R1, R10, R11, R12, R13, R14, R15, R16, R17, R18, R2, R26, R3, R32, R34, R35, R5, R6, R66, R67, R7, R74, R76, R77, R78, R8, R82, R86, R87, R88, R9, R92, R_IN1, R_IN2, R_IN3, R_IN4, R_LD1, R_SNS1, R_TS_PU1, SW1, SW2, TH1, U1, U10, U11, U12, U13, U15, U2, Y3: moved to B.Cu
- moved R3 305.0 mm to (101.0, 83.9)
- moved R82 299.0 mm to (105.0, 86.6), turned to 180 degrees
- moved R5 298.9 mm to (102.6, 83.9)
- moved C34 298.9 mm to (101.7, 78.7), turned to 90 degrees
- moved TH1 298.6 mm to (105.2, 88.3), turned to 180 degrees
- moved C5 297.8 mm to (106.0, 84.6), turned to 180 degrees
- moved C3 297.7 mm to (106.0, 82.9), turned to 180 degrees
- moved C33 297.0 mm to (103.2, 78.7), turned to 90 degrees
- moved C32 295.1 mm to (104.8, 78.7), turned to 90 degrees
- moved C16 294.6 mm to (107.1, 81.6), turned to 0 degrees
- moved R32 294.1 mm to (107.5, 87.1)
- moved C31 293.2 mm to (106.3, 78.7), turned to 90 degrees
- moved C27 291.4 mm to (107.9, 78.7), turned to 90 degrees
- moved C6 290.5 mm to (109.0, 80.8)
- moved R2 288.0 mm to (110.6, 88.5), turned to 180 degrees
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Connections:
- C30 pad 1: Net-(Q2-D) -> /Charger/V_in
- C4 pad 1: Net-(Q2-D) -> /Charger/V_in
- C7 pad 1: Net-(Q2-D) -> /Charger/V_in
- U2 pad 11: Net-(U2-ACDRV1) -> GND
- U2 pad 2: Net-(Q2-D) -> /Charger/V_in
- U2 pad 3: Net-(Q2-D) -> /Charger/V_in
- U2 pad 8: Net-(Q2-D) -> /Charger/V_in
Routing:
- net +3V3: track 18.4 -> 159.8 mm, vias 2 -> 24
- net I2C1_SCL: track 0.99 -> 81.7 mm, vias 0 -> 3
- net I2C1_SDA: track 0.98 -> 77.6 mm, vias 0 -> 3
- net +5V: track 7.15 -> 71.7 mm, vias 1 -> 4
- net SWDIO: track 0.00 -> 63.0 mm, vias 0 -> 2
- net main_voltage: track 0.00 -> 47.3 mm
- net SWO: track 0.00 -> 44.1 mm, vias 0 -> 2
- net SWCLK: track 0.00 -> 43.7 mm, vias 0 -> 2
- net charging_voltage: track 0.00 -> 43.0 mm
- net NRST: track 0.00 -> 41.3 mm
- net CHRG_IND_LED_4: track 0.00 -> 37.8 mm, vias 0 -> 4
- net /Charger/CE_N: track 5.09 -> 42.7 mm, vias 0 -> 1
- net BOOT: track 0.00 -> 35.8 mm
- net CAN-: track 0.00 -> 30.5 mm
- net CHRG_IND_LED_1: track 0.00 -> 30.4 mm
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- added copper zone on B.Cu, net +3V3
- added copper zone on F.Cu, net +3V3
- added copper zone on B.Cu, net +5V
- added copper zone on F.Cu, net GND
- added copper zone on In1.Cu, net GND
- added copper zone on In2.Cu, net GND
- added copper zone on B.Cu, net Net-(D10-K)
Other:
- board size 97 x 82 mm -> 78 x 104 mm
- board text added: "+"
- board text added: "-"
- board text added: "Boot"
- board text added: "Circumvent"
- board text added: "HCO1"
- board text added: "HCO2"
- board text added: "HCO3"
- board text added: "Main Switch"
- board text added: "Reset"
- board text added: "Vehicle Bus1"
- board text added: "Vehicle Bus2"
- board text added: "match SRN and SRP traces"
- board text removed: "Arming"
- board text removed: "HCO"
- board text removed: "Vehicle Bus"
